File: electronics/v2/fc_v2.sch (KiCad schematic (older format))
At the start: 45 parts, among them J1 Conn_02x03_Counter_Clockwise, Q1 Q_NPN, SW1 SW_DPST_x2, U1 teensy4, U10 terminal-2, U11 BTN7030-1EPA, U12 BTN7030-1EPA, U13 BTN7030-1EPA, U14 BTN7030-1EPA, U2 RFM69HCW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

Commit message: fixes on PCB
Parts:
- added D1: D_Schottky, Diode_SMD:D_0805_2012Metric_Pad1.15x1.40mm_HandSolder, symbol Device:D_Schottky
- added H1, H2, H4, H5: MountingHole, MountingHole:MountingHole_2.2mm_M2_ISO7380, symbol Mechanical:MountingHole
- added H3: Logo, custom:avatar, symbol Mechanical:MountingHole
- added R6: 10k, Resistor_SMD:R_0805_2012Metric_Pad1.20x1.40mm_HandSolder, symbol Device:R
- added R7: 4.7k, Resistor_SMD:R_0805_2012Metric_Pad1.20x1.40mm_HandSolder, symbol Device:R
- added R9: 2k, Resistor_SMD:R_0805_2012Metric_Pad1.20x1.40mm_HandSolder, symbol Device:R
- C2: value 22pF -> 100pF
- R14, R15: value 330 -> 700
- R16: value 10k -> 2k
- U4: footprint Package_SO:SOIC-8_7.5x5.85mm_P1.27mm -> Package_SO:SOIC-8_5.275x5.275mm_P1.27mm
- U5: footprint Connector_AMASS:AMASS_XT30U-F_1x02_P5.0mm_Vertical -> Connector_AMASS:AMASS_XT30U-M_1x02_P5.0mm_Vertical
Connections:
- net 3V3: now also U4.3 (WP), U4.7 (HOLD)
- net 5V: now also D1.1 (K); no longer C4.1, U6.3 (VO)
- net BUZZ: now also R6.1, R9.2; no longer Q1.1 (B)
- net GND: now also R6.2; no longer U4.3 (WP), U4.7 (HOLD)
- net P-EN: now also R7.2; no longer R16.1, SW1.2 (B)
- new net: C4.1, D1.2 (A), U6.3 (VO)
- new net: Q1.1 (B), R9.1
- new net: R16.1, R7.1, SW1.2 (B)
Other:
- note added: "Mechanical"
- moved on the sheet: J1

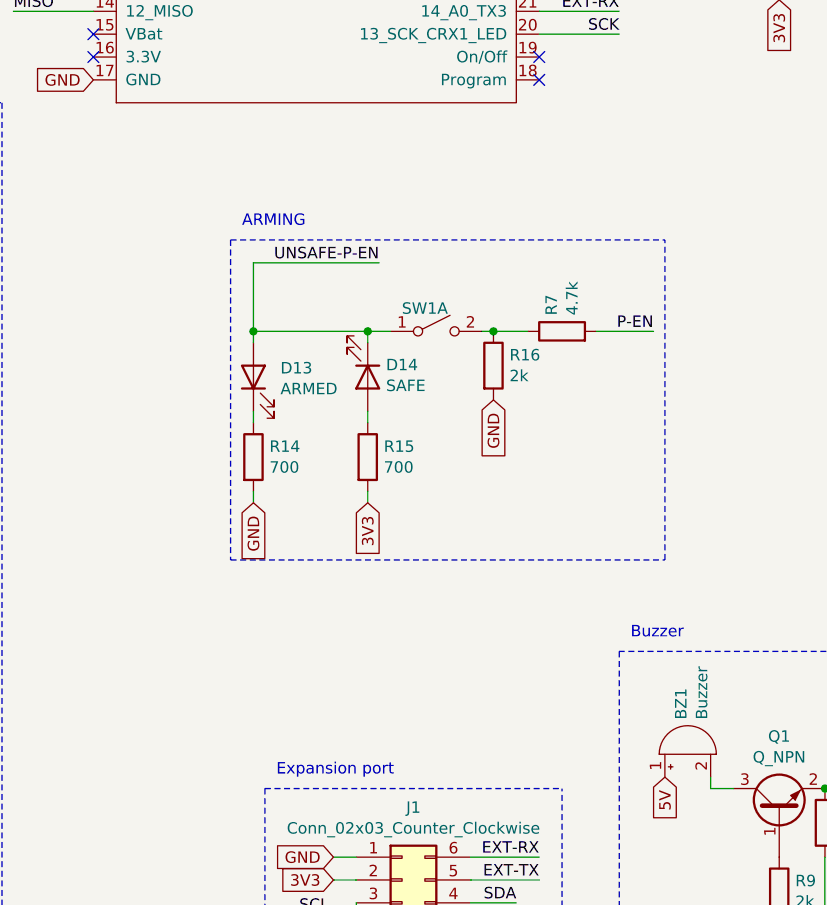
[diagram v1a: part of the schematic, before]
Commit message: fix P-EN
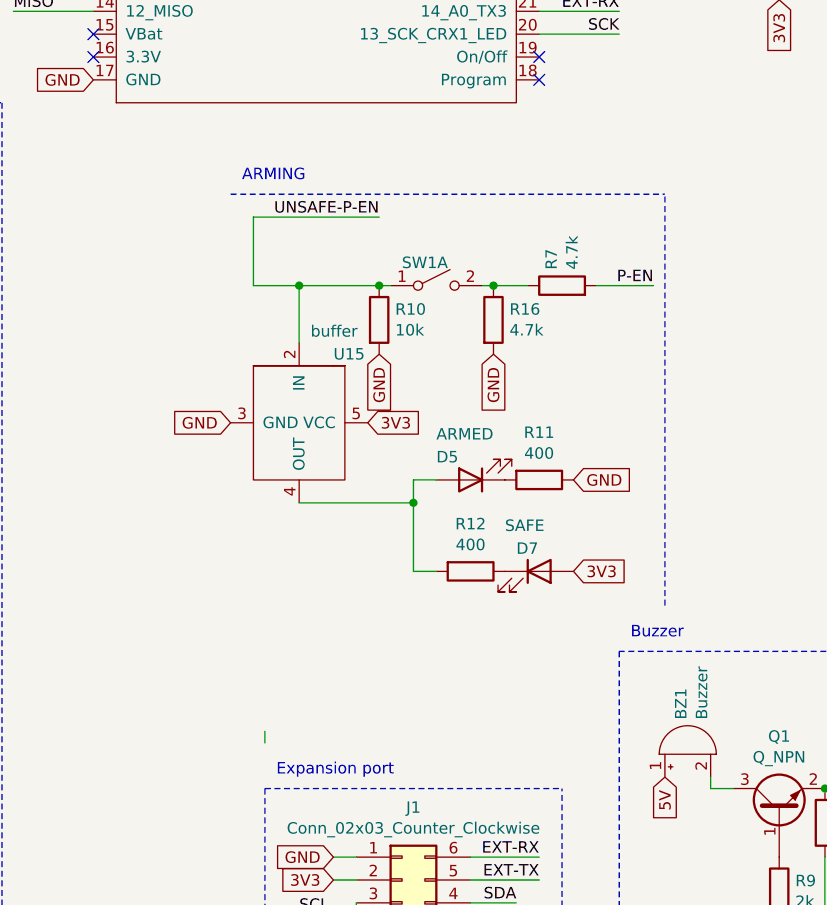
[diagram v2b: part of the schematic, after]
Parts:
- removed D13: ARMED, LED_SMD:LED_0805_2012Metric_Pad1.15x1.40mm_HandSolder, symbol Device:LED
- removed D14: SAFE, LED_SMD:LED_0805_2012Metric_Pad1.15x1.40mm_HandSolder, symbol Device:LED
- removed R14, R15: 700, Resistor_SMD:R_0805_2012Metric_Pad1.20x1.40mm_HandSolder, symbol Device:R
- added D5: ARMED, LED_SMD:LED_0805_2012Metric_Pad1.15x1.40mm_HandSolder, symbol Device:LED
- added D7: SAFE, LED_SMD:LED_0805_2012Metric_Pad1.15x1.40mm_HandSolder, symbol Device:LED
- added R10: 10k, Resistor_SMD:R_0805_2012Metric_Pad1.20x1.40mm_HandSolder, symbol Device:R
- added R11, R12: 400, Resistor_SMD:R_0805_2012Metric_Pad1.20x1.40mm_HandSolder, symbol Device:R
- added U15: buffer, custom:SC-74-a, symbol custom:buffer
- R16: value 2k -> 4.7k
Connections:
- net 3V3: now also D7.2 (A), U15.5 (VCC)
- net GND: now also R10.2, R11.1, U15.3 (GND)
- net UNSAFE-P-EN: now also R10.1, U15.2 (IN)
- new net: D5.2 (A), R12.2, U15.4 (OUT)
- new net: D7.1 (K), R12.1
- new net: D5.1 (K), R11.2
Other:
- moved on the sheet: R16, R7, SW1A
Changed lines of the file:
@@
 Text Label 4300 1900 0    50   ~ 0
 P-IN-3
-Text Label 7100 3800 2    50   ~ 0
+Text Label 7100 3600 2    50   ~ 0
 P-EN
 Wire Notes Line
@@
 Wire Wire Line
 	6950 2500 6600 2500
-Wire Wire Line
-	5350 3500 5350 3800
-Text GLabel 6400 4100 3    50   Input ~ 0
+Text GLabel 6400 3900 3    50   Input ~ 0
 GND
 Wire Notes Line
@@
 	1250 4650 1900 4650
 Wire Wire Line
-	6400 3800 6350 3800
-Wire Wire Line
-	5850 4150 5850 4200
-Wire Wire Line
-	5350 4150 5350 4200
-Wire Wire Line
-	5350 3800 5850 3800
-Wire Wire Line
-	5350 3850 5350 3800
-Connection ~ 5350 3800
-Wire Wire Line
-	5850 3850 5850 3800
-Connection ~ 5850 3800
-Wire Wire Line
-	5850 3800 5950 3800
-Text GLabel 5350 4550 3    50   Input ~ 0
-GND
-Text GLabel 5850 4550 3    50   Input ~ 0
-3V3
-Wire Wire Line
-	5850 4550 5850 4500
-Wire Wire Line
-	5350 4550 5350 4500
+	6400 3600 6350 3600
+Wire Wire Line
+	5400 5600 5400 5550
 Wire Notes Line
 	9250 5300 11050 5300
@@
 Text Notes 7000 5150 0    50   ~ 0
 Buzzer
-Text Label 5900 3500 2    50   ~ 0
+Text Label 5900 3300 2    50   ~ 0
 UNSAFE-P-EN
 Wire Wire Line
-	5350 3500 5900 3500
-Wire Notes Line
-	7150 4800 7150 3400
-Wire Notes Line
-	5250 3400 5250 4800
-Text Notes 5300 3350 0    50   ~ 0
+	5350 3300 5900 3300
+Wire Notes Line
+	7150 5000 7150 3200
+Text Notes 5300 3150 0    50   ~ 0
 ARMING
 Text Notes 700  2750 0    50   ~ 0
@@
 	7850 6100 7850 6400
 Wire Notes Line
-	5250 4800 7150 4800
-Wire Notes Line
-	5250 3400 7150 3400
-Wire Wire Line
-	7100 3800 6850 3800
-Wire Wire Line
-	6550 3800 6400 3800
-Connection ~ 6400 3800
+	5250 3200 7150 3200
+Wire Wire Line
+	7100 3600 6850 3600
+Wire Wire Line
+	6550 3600 6400 3600
+Connection ~ 6400 3600
 Connection ~ 2250 1150
 Wire Wire Line
@@
 L Switch:SW_DPST_x2 SW1
 U 1 1 61298F6A
-P 6150 3800
-F 0 "SW1" H 6100 3900 50  0000 C CNN
-F 1 "SW_DPST_x2" H 6150 3944 50  0001 C CNN
-F 2 "Connector_PinHeader_2.54mm:PinHeader_1x02_P2.54mm_Vertical" H 6150 3800 50  0001 C CNN
-F 3 "~" H 6150 3800 50  0001 C CNN
-	1    6150 3800
-	1    0    0    -1
-$EndComp
-$Comp
-L Device:LED D13
-U 1 1 6136C6E9
-P 5350 4000
-F 0 "D13" V 5389 3882 50  0000 R CNN
-F 1 "ARMED" V 5298 3882 50  0000 R CNN
-F 2 "LED_SMD:LED_0805_2012Metric_Pad1.15x1.40mm_HandSolder" H 5350 4000 50  0001 C CNN
-F 3 "~" H 5350 4000 50  0001 C CNN
-	1    5350 4000
-	0    -1   -1   0
+P 6150 3600
+F 0 "SW1" H 6100 3700 50  0000 C CNN
+F 1 "SW_DPST_x2" H 6150 3744 50  0001 C CNN
+F 2 "Connector_PinHeader_2.54mm:PinHeader_1x02_P2.54mm_Vertical" H 6150 3600 50  0001 C CNN
+F 3 "~" H 6150 3600 50  0001 C CNN
+	1    6150 3600
+	1    0    0    -1
 $EndComp
 $Comp
 L Device:R R16
 U 1 1 61396871
-P 6400 3950
-F 0 "R16" H 6470 3996 50  0000 L CNN
-F 1 "2k" H 6470 3905 50  0000 L CNN
-F 2 "Resistor_SMD:R_0805_2012Metric_Pad1.20x1.40mm_HandSolder" V 6330 3950 50  0001 C CNN
-F 3 "~" H 6400 3950 50  0001 C CNN
-	1    6400 3950
-	1    0    0    -1
-$EndComp
-$Comp
-L Device:LED D14
-U 1 1 614BDDC7
-P 5850 4000
-F 0 "D14" V 5797 4080 50  0000 L CNN
-F 1 "SAFE" V 5888 4080 50  0000 L CNN
-F 2 "LED_SMD:LED_0805_2012Metric_Pad1.15x1.40mm_HandSolder" H 5850 4000 50  0001 C CNN
-F 3 "~" H 5850 4000 50  0001 C CNN
-	1    5850 4000
-	0    1    1    0
-$EndComp
-$Comp
-L Device:R R14
-U 1 1 61554446
-P 5350 4350
-F 0 "R14" H 5420 4396 50  0000 L CNN
-F 1 "700" H 5420 4305 50  0000 L CNN
-F 2 "Resistor_SMD:R_0805_2012Metric_Pad1.20x1.40mm_HandSolder" V 5280 4350 50  0001 C CNN
-F 3 "~" H 5350 4350 50  0001 C CNN
-	1    5350 4350
-	1    0    0    -1
-$EndComp
-$Comp
-L Device:R R15
-U 1 1 615554FE
-P 5850 4350
-F 0 "R15" H 5920 4396 50  0000 L CNN
-F 1 "700" H 5920 4305 50  0000 L CNN
-F 2 "Resistor_SMD:R_0805_2012Metric_Pad1.20x1.40mm_HandSolder" V 5780 4350 50  0001 C CNN
-F 3 "~" H 5850 4350 50  0001 C CNN
-	1    5850 4350
+P 6400 3750
+F 0 "R16" H 6470 3796 50  0000 L CNN
+F 1 "4.7k" H 6470 3705 50  0000 L CNN
+F 2 "Resistor_SMD:R_0805_2012Metric_Pad1.20x1.40mm_HandSolder" V 6330 3750 50  0001 C CNN
+F 3 "~" H 6400 3750 50  0001 C CNN
+	1    6400 3750
 	1    0    0    -1
 $EndComp
@@
 L Device:R R7
 U 1 1 60E0DAC5
-P 6700 3800
-F 0 "R7" H 6770 3846 50  0000 L CNN
-F 1 "4.7k" H 6770 3755 50  0000 L CNN
-F 2 "Resistor_SMD:R_0805_2012Metric_Pad1.20x1.40mm_HandSolder" V 6630 3800 50  0001 C CNN
-F 3 "~" H 6700 3800 50  0001 C CNN
-	1    6700 3800
+P 6700 3600
+F 0 "R7" H 6770 3646 50  0000 L CNN
+F 1 "4.7k" H 6770 3555 50  0000 L CNN
+F 2 "Resistor_SMD:R_0805_2012Metric_Pad1.20x1.40mm_HandSolder" V 6630 3600 50  0001 C CNN
+F 3 "~" H 6700 3600 50  0001 C CNN
+	1    6700 3600
 	0    -1   -1   0
 $EndComp
@@
 $EndComp
 NoConn ~ 9700 4900
+Wire Wire Line
+	5350 3600 5550 3600
+Text GLabel 5900 3900 3    50   Input ~ 0
+GND
+$Comp
+L Device:R R10
+U 1 1 60D2E25B
+P 5900 3750
+F 0 "R10" H 5970 3796 50  0000 L CNN
+F 1 "10k" H 5970 3705 50  0000 L CNN
+F 2 "Resistor_SMD:R_0805_2012Metric_Pad1.20x1.40mm_HandSolder" V 5830 3750 50  0001 C CNN
+F 3 "~" H 5900 3750 50  0001 C CNN
+	1    5900 3750
+	1    0    0    -1
+$EndComp
+$Comp
+L custom:buffer U15
+U 1 1 60DC1EDD
+P 5500 4100
+F 0 "U15" V 5300 4300 50  0000 L CNN
+F 1 "buffer" V 5200 4200 50  0000 L CNN
+F 2 "custom:SC-74-a" H 5300 4350 50  0001 C CNN
+F 3 "" H 5300 4350 50  0001 C CNN
+	1    5500 4100
+	0    1    1    0
+$EndComp
+Wire Wire Line
+	5550 3850 5550 3600
+Connection ~ 5550 3600
+Wire Wire Line
+	5550 3600 5900 3600
+Text GLabel 5250 4200 0    50   Input ~ 0
+GND
+Text GLabel 5850 4200 2    50   Input ~ 0
+3V3
+$Comp
+L Device:LED D7
+U 1 1 60DFFEAA
+P 6600 4850
+F 0 "D7" H 6500 4950 50  0000 L CNN
+F 1 "SAFE" H 6450 5050 50  0000 L CNN
+F 2 "LED_SMD:LED_0805_2012Metric_Pad1.15x1.40mm_HandSolder" H 6600 4850 50  0001 C CNN
+F 3 "~" H 6600 4850 50  0001 C CNN
+	1    6600 4850
+	1    0    0    -1
+$EndComp
+$Comp
+L Device:R R11
+U 1 1 60E1E942
+P 6600 4450
+F 0 "R11" V 6393 4450 50  0000 C CNN
+F 1 "400" V 6484 4450 50  0000 C CNN
+F 2 "Resistor_SMD:R_0805_2012Metric_Pad1.20x1.40mm_HandSolder" V 6530 4450 50  0001 C CNN
+F 3 "~" H 6600 4450 50  0001 C CNN
+	1    6600 4450
+	0    1    1    0
+$EndComp
+$Comp
+L Device:LED D5
+U 1 1 60E5C291
+P 6300 4450
+F 0 "D5" H 6450 4350 50  0000 R CNN
+F 1 "ARMED" H 6450 4250 50  0000 R CNN
+F 2 "LED_SMD:LED_0805_2012Metric_Pad1.15x1.40mm_HandSolder" H 6300 4450 50  0001 C CNN
+F 3 "~" H 6300 4450 50  0001 C CNN
+	1    6300 4450
+	-1   0    0    1
+$EndComp
+Wire Wire Line
+	6150 4850 6050 4850
+Text GLabel 6750 4450 2    50   Input ~ 0
+GND
+Wire Wire Line
+	6050 4850 6050 4550
+Wire Wire Line
+	6050 4450 6150 4450
+Connection ~ 6050 4550
+Wire Wire Line
+	6050 4550 6050 4450
+Wire Wire Line
+	5550 4550 6050 4550
+Connection ~ 5900 3600
+Wire Wire Line
+	5900 3600 5950 3600
+Wire Wire Line
+	5350 3300 5350 3600
+$Comp
+L Device:R R12
+U 1 1 60F93FFE
+P 6300 4850
+F 0 "R12" V 6093 4850 50  0000 C CNN
+F 1 "400" V 6184 4850 50  0000 C CNN
+F 2 "Resistor_SMD:R_0805_2012Metric_Pad1.20x1.40mm_HandSolder" V 6230 4850 50  0001 C CNN
+F 3 "~" H 6300 4850 50  0001 C CNN
+	1    6300 4850
+	0    1    1    0
+$EndComp
+Text GLabel 6750 4850 2    50   Input ~ 0
+3V3
 $EndSCHEMATC

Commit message: main fc traces done
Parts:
- removed J1: Conn_02x03_Counter_Clockwise, Connector_PinHeader_2.54mm:PinHeader_2x03_P2.54mm_Vertical, symbol Connector_Generic:Conn_02x03_Counter_Clockwise
- removed Q1: Q_NPN, Package_TO_SOT_SMD:SOT-23, symbol custom:Q_NPN
- removed U4: W25Q128JV, Package_SO:SOIC-8_5.275x5.275mm_P1.27mm, symbol custom:W25Q128JV
- added C1: 100nF, Capacitor_SMD:C_0805_2012Metric_Pad1.18x1.45mm_HandSolder, symbol Device:C
- added C9: C, Capacitor_SMD:C_0805_2012Metric_Pad1.18x1.45mm_HandSolder, symbol Device:C
- added D11, D9: D_Schottky, Diode_SMD:D_0805_2012Metric_Pad1.15x1.40mm_HandSolder, symbol Device:D_Schottky
- added H6: Aesir, custom:aesir, symbol Mechanical:MountingHole
- added J1: Conn_02x03_Odd_Even, Connector_PinHeader_2.54mm:PinHeader_2x03_P2.54mm_Vertical, symbol Connector_Generic:Conn_02x03_Odd_Even
- added J2: JST_XH_4, Connector_JST:JST_XH_B4B-XH-A_1x04_P2.50mm_Vertical, symbol Connector_Generic:Conn_01x04
- added Q1: MMBT3904, Package_TO_SOT_SMD:SOT-23, symbol Transistor_BJT:MMBT3904
- added R13: 120, Resistor_SMD:R_0805_2012Metric_Pad1.20x1.40mm_HandSolder, symbol Device:R
- added U16: w25nxx, Package_SO:SOIC-16W_7.5x10.3mm_P1.27mm, symbol custom:w25nxx
- added U4: SN65HVD230, Package_SO:SOIC-8_3.9x4.9mm_P1.27mm, symbol Interface_CAN_LIN:SN65HVD230
- BZ1: footprint custom:buzzer -> custom:CX-0905C
- R9: value 2k -> 1k
- U15: value buffer -> NL17SZ17
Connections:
- net 3V3: now also C1.2, U16.1 (RESET), U16.2 (VCC), U16.3 (RESET), U16.9 (WP), U4.3 (VCC)
- net 5V: now also D11.2 (A), D9.1 (K)
- net MISO: now also U16.8 (DO)
- net MOSI: now also U16.15 (DI)
- net SCK: now also U16.16 (CLK)
- net SCL: now also J1.3 (Pin_3)
- net SDA: now also J1.4 (Pin_4)
- net CAN_RX: now reaches U1.2 (0_RX1_CRX2)
- net CAN_RX: now also U4.4 (R)
- net CAN_TX: now reaches U1.3 (1_TX1_CTX2)
- net CAN_TX: now also U4.1 (D)
- net at BZ1.2 (+): now also Q1.3 (C)
- net at R9.1: now also Q1.1 (B)
- net at D2.3 (VSS), D3.1 (K): now also C9.1
- net BAT-READ renamed BAT_READ
- net EXT-RX renamed EXT_RX
- net EXT_RX: now also J1.6 (Pin_6)
- net EXT-TX renamed EXT_TX
- net EXT_TX: now also J1.5 (Pin_5)
- net FLASH-CS renamed FLASH_CS
- net FLASH_CS: now also U16.7 (CS)
- net GND renamed Earth
- net Earth: now also C1.1, C9.2, J1.1 (Pin_1), J2.4 (Pin_4), Q1.2 (E), U16.10 (GND), U4.2 (GND), U4.8 (Rs)
- net P-EN renamed P_EN
- net P-IN-1 renamed P_IN_1
- net P-IN-2 renamed P_IN_2
- net P-IN-3 renamed P_IN_3
- net P-IN-4 renamed P_IN_4
- net RF-CS renamed RF_CS
- net RF-G0 renamed RF_G0
- net RF-RST renamed RF_RST
- net UNSAFE-P-EN renamed UNSAFE_P_EN
- new net: D11.1 (K), J1.2 (Pin_2)
- new net: J2.3 (Pin_3), R13.2, U4.6 (CANL)
- new net: J2.2 (Pin_2), R13.1, U4.7 (CANH)
- new net: D9.2 (A), J2.1 (Pin_1)
- no-connect marks 15 -> 13
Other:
- note added: "CAN\n"
- moved on the sheet: BZ1, C2, D5, D7, H1, H2, H3, H4, H5, R10, R11, R12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

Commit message: pre routing mini controller
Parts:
- removed D3: D_Schottky, Diode_SMD:D_0805_2012Metric_Pad1.15x1.40mm_HandSolder, symbol Device:D_Schottky
- removed H1, H2, H4, H5: MountingHole, MountingHole:MountingHole_2.2mm_M2_ISO7380, symbol Mechanical:MountingHole
- removed R16: 4.7k, Resistor_SMD:R_0805_2012Metric_Pad1.20x1.40mm_HandSolder, symbol Device:R
- added H1, H2, H4, H5: MountingHole_Pad, MountingHole:MountingHole_2.2mm_M2_Pad_Via, symbol Mechanical:MountingHole_Pad
- added JP1: Jumper_NC_Small, Connector_PinHeader_2.54mm:PinHeader_1x02_P2.54mm_Vertical, symbol Device:Jumper_NC_Small
- added JP2: Jumper, Connector_JST:JST_XH_B2B-XH-A_1x02_P2.50mm_Vertical, symbol Device:Jumper_NO_Small
- added JP3: Jumper_NO_Small, custom:R_1812_4532Metric_Pad1.30x3.40mm_HandSolder_no_silk, symbol Device:Jumper_NO_Small
- added R14: 1k, Resistor_SMD:R_0805_2012Metric_Pad1.20x1.40mm_HandSolder, symbol Device:R
- added R15: 2k, Resistor_SMD:R_0805_2012Metric_Pad1.20x1.40mm_HandSolder, symbol Device:R
- added U17: NL17SZ17, custom:SC-74-a, symbol custom:buffer
- C1: value 100nF -> 100n
- C2: value 100pF -> 100p
- C3: value 20uF -> 20u
- C4: value 10uF -> 10u
- C9: value C -> 100n
- D1, D11, D4, D9: footprint Diode_SMD:D_0805_2012Metric_Pad1.15x1.40mm_HandSolder -> Diode_SMD:D_SOD-323_HandSoldering
- R1: value 6k -> 6.04k
- R10: value 10k -> 4.7k
- R7: value 4.7k -> 1k
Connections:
- net 12V: now also JP3.1; no longer C10.2, C12.2, U11.15 (VS), U12.15 (VS), U13.15 (VS), U14.15 (VS)
- net 3V3: now also JP2.2
- net 5V: now also C9.1, D2.3 (VSS), U17.5 (VCC)
- net Earth: now also J2.3 (Pin_3), SW1.1 (A), H1.1, H2.1, H4.1, H5.1, R15.2, U17.3 (GND); no longer J2.4 (Pin_4)
- net UNSAFE_P_EN: now also R14.1; no longer SW1.1 (A)
- net RGB_TX: now reaches U1.27 (20_A6_TX5_NO_PWM)
- net RGB_TX: now also U17.2 (IN)
- net LIFTOFF: now reaches U1.29 (22_A8_CTX1)
- net LIFTOFF: now also JP2.1, R15.1
- net at R7.1, SW1.2 (B): now also R14.2
- net at R13.1, U4.7 (CANH): now also J2.1 (Pin_1); no longer J2.2 (Pin_2)
- net at D9.2 (A): now also J2.4 (Pin_4); no longer J2.1 (Pin_1)
- net RGB: no longer names the net of U1.4 (2)
- net RGB: no longer D2.4 (DIN)
- new net: D2.4 (DIN), U17.4 (OUT)
- new net: J2.2 (Pin_2), JP1.2, U4.6 (CANL)
- new net: JP1.1, R13.2
- new net 12V_LIMIT: C10.2, C12.2, JP3.2, U11.15 (VS), U12.15 (VS), U13.15 (VS), U14.15 (VS)
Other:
- moved on the sheet: C9, D2, D9, J2, R13, R7
